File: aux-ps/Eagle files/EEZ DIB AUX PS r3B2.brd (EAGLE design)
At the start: 230.5 x 60 mm, 85 parts, among them IC1 BD00FC0WFP, IC2 MAX31760AEE+, J1 PF0030/PC, J2 4907, J3 4907, J4 4907, J5 SWEB 8094 AU/GN, Q1 BTA26-600, Q2 BTA26-600, Q3 2N7002, Q4 2N7002, Q5 2N7002, SW1 DF62J12S2AHQA, SW2 OS102011MA1QN1C, X1 39-28-1063, X2 39-30-1039, X3 DS1013-16SSIB1, X4 47053-1000, X5 47053-1000

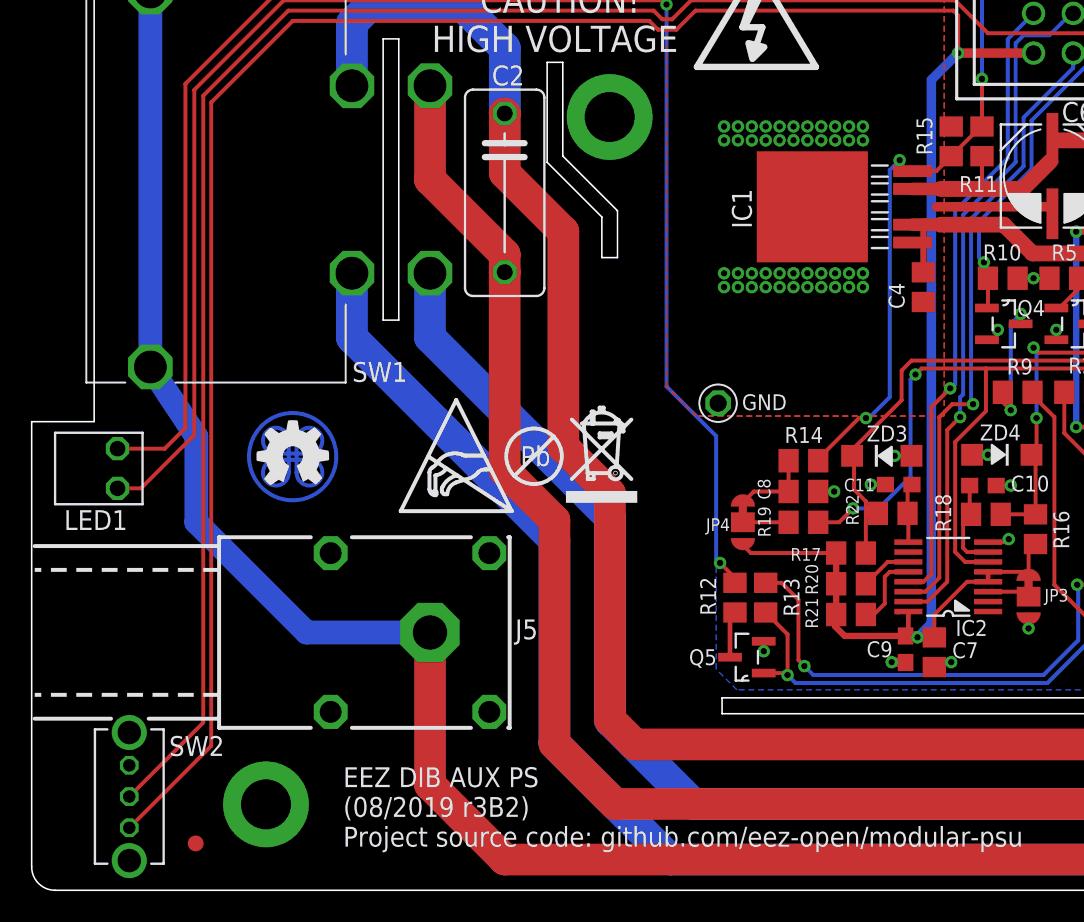
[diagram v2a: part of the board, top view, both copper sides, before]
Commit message: multiple PCB layout adjustments
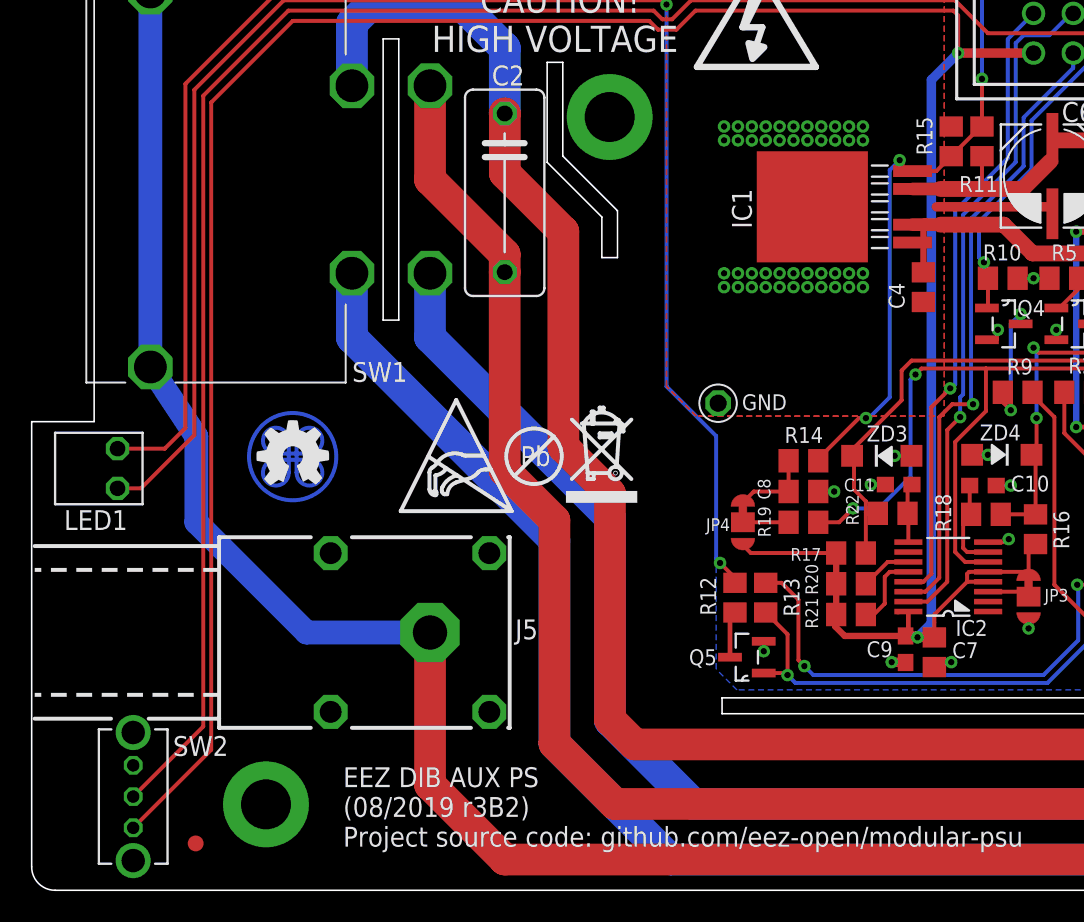
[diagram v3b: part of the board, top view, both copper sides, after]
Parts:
- moved SW2 0.25 mm to (6.50, 6.00)
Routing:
- net +3V3: track 177.1 -> 178.3 mm
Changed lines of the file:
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@@
 <layer number="27" name="tValues" color="14" fill="1" visible="no" active="yes"/>
 <layer number="28" name="bValues" color="11" fill="1" visible="yes" active="yes"/>
-<layer number="29" name="tStop" color="15" fill="1" visible="no" active="yes"/>
+<layer number="29" name="tStop" color="15" fill="1" visible="yes" active="yes"/>
 <layer number="30" name="bStop" color="7" fill="1" visible="yes" active="yes"/>
 <layer number="31" name="tCream" color="7" fill="4" visible="no" active="yes"/>
@@
 <layer number="49" name="Reference" color="7" fill="1" visible="no" active="yes"/>
 <layer number="50" name="dxf" color="7" fill="1" visible="no" active="no"/>
-<layer number="51" name="tDocu" color="14" fill="1" visible="no" active="yes"/>
+<layer number="51" name="tDocu" color="14" fill="1" visible="yes" active="yes"/>
 <layer number="52" name="bDocu" color="7" fill="1" visible="no" active="yes"/>
 <layer number="53" name="tGND_GNDA" color="7" fill="9" visible="no" active="no"/>
@@
 <wire x1="44.196" y1="12.319" x2="71.6915" y2="12.319" width="0.1016" layer="20"/>
 <wire x1="44.196" y1="11.303" x2="44.196" y2="12.319" width="0.1016" layer="20"/>
-<rectangle x1="84.8995" y1="0.889" x2="148.844" y2="5.588" layer="51"/>
 <wire x1="43.815" y1="14.224" x2="43.815" y2="29.083" width="0.254" layer="51"/>
 <wire x1="43.815" y1="29.083" x2="40.64" y2="32.258" width="0.254" layer="51"/>
 <wire x1="40.64" y1="32.258" x2="40.64" y2="35.433" width="0.254" layer="51"/>
+<dimension x1="0" y1="-13.5" x2="4" y2="1" x3="2" y3="-12.5" textsize="2" layer="47" dtype="horizontal"/>
 </plain>
 <attributes>
@@
 <attribute name="VALUE" x="128.1525" y="29.2345" size="2.1844" layer="27" ratio="10"/>
 </element>
-<element name="SW2" library="EEZ_switches" package="OS102011" value="OS102011MA1QN1C" x="6.25" y="6" locked="yes" smashed="yes" rot="R270">
-<attribute name="NAME" x="8.7955" y="8.5995" size="1.27" layer="25" ratio="10"/>
-<attribute name="VALUE" x="1.9375" y="5.361" size="1.27" layer="27" ratio="10"/>
+<element name="SW2" library="EEZ_switches" package="OS102011" value="OS102011MA1QN1C" x="6.5" y="6" locked="yes" smashed="yes" rot="R270">
+<attribute name="NAME" x="9.0455" y="8.5995" size="1.27" layer="25" ratio="10"/>
+<attribute name="VALUE" x="2.1875" y="5.361" size="1.27" layer="27" ratio="10"/>
 </element>
 <element name="D1" library="EEZ_Lib1" package="SOD123" value="SKL16" x="121.0945" y="56.5785" smashed="yes" rot="R270">
@@
 <contactref element="IC2" pad="5"/>
 <contactref element="JP3" pad="NC"/>
-<wire x1="61.2267" y1="20.3835" x2="61.2267" y2="19.7485" width="0.3048" layer="1"/>
 <wire x1="51.501" y1="21.59" x2="51.501" y2="19.6215" width="0.4064" layer="1"/>
 <wire x1="51.501" y1="19.6215" x2="51.501" y2="17.653" width="0.4064" layer="1"/>
 <contactref element="SW2" pad="3"/>
-<wire x1="6.25" y1="4" x2="11.4935" y2="9.2435" width="0.254" layer="1"/>
 <contactref element="JP4" pad="NO"/>
 <contactref element="X3" pad="16"/>
@@
 <wire x1="51.435" y1="17.587" x2="51.501" y2="17.653" width="0.4064" layer="1"/>
 <wire x1="56.0705" y1="17.7927" x2="56.1213" y2="17.8435" width="0.3048" layer="1"/>
-<wire x1="11.4935" y1="9.2435" x2="11.4935" y2="50.4317" width="0.254" layer="1"/>
+<wire x1="11.4935" y1="8.9935" x2="11.4935" y2="50.4317" width="0.254" layer="1"/>
 <wire x1="11.4935" y1="50.4317" x2="16.7132" y2="55.6514" width="0.254" layer="1"/>
 <wire x1="16.7132" y1="55.6514" x2="39.5351" y2="55.6514" width="0.254" layer="1"/>
@@
 <wire x1="57.5945" y1="51.8795" x2="59.309" y2="53.594" width="0.6096" layer="16"/>
 <wire x1="57.5945" y1="17.0815" x2="56.7055" y2="16.1925" width="0.6096" layer="16"/>
+<wire x1="11.4935" y1="8.9935" x2="6.5" y2="4" width="0.254" layer="1"/>
+<wire x1="61.2267" y1="20.3835" x2="60.0075" y2="20.3835" width="0.254" layer="1"/>
+<wire x1="60.0075" y1="20.3835" x2="59.8805" y2="20.2565" width="0.254" layer="1"/>
+<wire x1="59.8805" y1="20.2565" x2="59.8805" y2="19.7485" width="0.254" layer="1"/>
 </signal>
 <signal name="SSCL">
@@
 <contactref element="SW2" pad="2"/>
 <contactref element="X3" pad="2"/>
-<wire x1="10.9855" y1="10.7355" x2="10.9855" y2="50.8635" width="0.254" layer="1"/>
-<wire x1="10.9855" y1="10.7355" x2="6.25" y2="6" width="0.254" layer="1"/>
+<wire x1="10.9855" y1="10.4855" x2="10.9855" y2="50.8635" width="0.254" layer="1"/>
 <wire x1="10.9855" y1="50.8635" x2="16.4338" y2="56.3118" width="0.254" layer="1"/>
 <wire x1="16.4338" y1="56.3118" x2="39.8145" y2="56.3118" width="0.254" layer="1"/>
@@
 <wire x1="61.214" y1="54.864" x2="59.1058" y2="56.9722" width="0.254" layer="1"/>
 <wire x1="42.2148" y1="56.9722" x2="59.1058" y2="56.9722" width="0.254" layer="1"/>
+<wire x1="10.9855" y1="10.4855" x2="6.5" y2="6" width="0.254" layer="1"/>
 </signal>
 <signal name="12V_PWM">

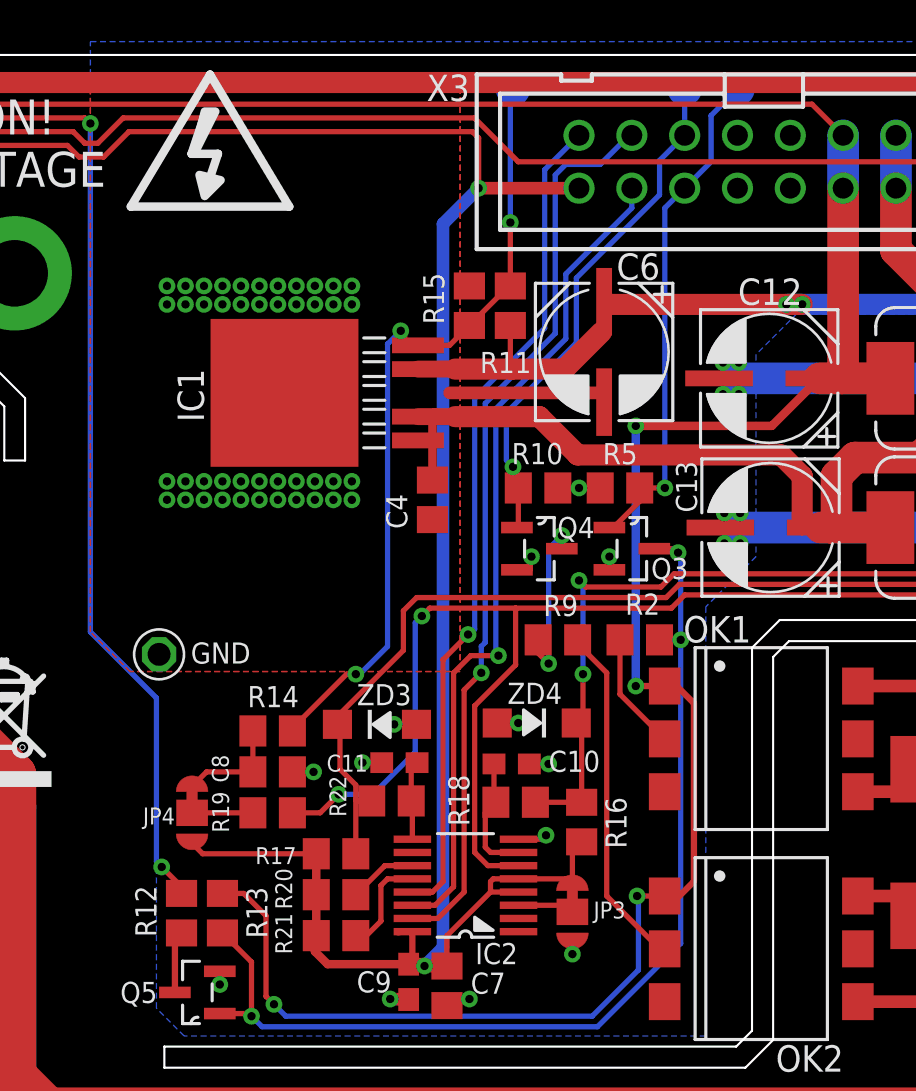
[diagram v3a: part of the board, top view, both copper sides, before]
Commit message: Fan LDO control fixed
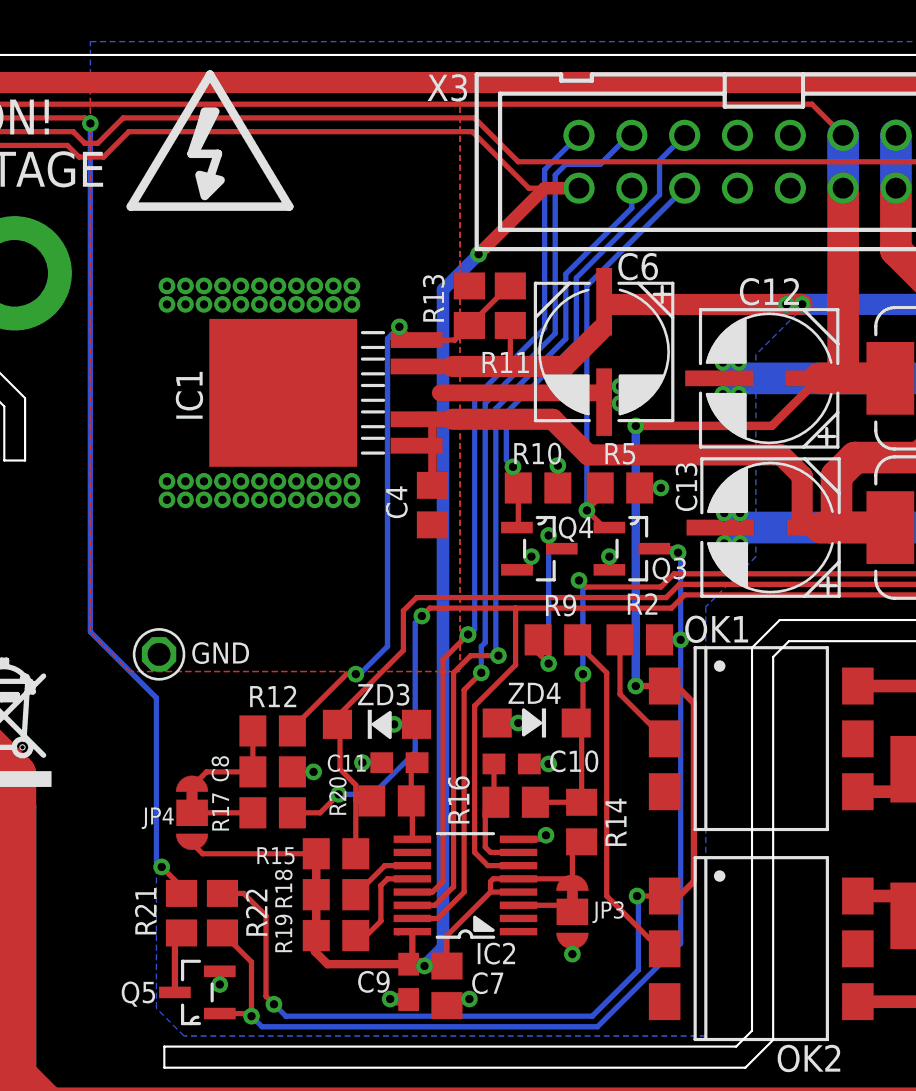
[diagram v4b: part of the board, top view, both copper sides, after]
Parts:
- removed DIR, FB, SS: (no value), EEZ_Lib1:PCB_TEST_PAD
- D1: value SKL16 -> SKL14
- IC1: value BD00FC0WFP -> BD00FC0WFP-E2; device EEZ_DIB:KVU5 -> EEZ_DIB:TO-252-5
- R11: value 10K -> 39K
- R12: value 470R -> 12K
- R13: value 47K -> 3K3
- R14: value 47K -> 1K
- R15: value 4K7 -> 1K
- R16: value 1K -> 10R
- R18: value 10R -> 4K7
- R19: value 1K -> N.C.
- R20: value 4K7 -> 10R
- R21: value N.C. -> 470R
- R22: value 10R -> 47K
- moved R13 31.5 mm to (58.9, 47.9), turned to 90 degrees
- moved R15 27.1 mm to (52.5, 21.6), turned to 180 degrees
- moved R14 15.5 mm to (64.3, 23.1), turned to 270 degrees
- moved R12 9.80 mm to (49.4, 27.5), turned to 180 degrees
- moved R22 9.76 mm to (47.0, 18.7), turned to 270 degrees
- moved R18 9.71 mm to (52.5, 19.6), turned to 180 degrees
- moved R21 7.51 mm to (45.0, 18.7), turned to 270 degrees
- moved R19 6.65 mm to (52.5, 17.7), turned to 180 degrees
- moved R20 5.24 mm to (55.1, 24.1)
- moved R17 3.63 mm to (49.4, 23.6), turned to 0 degrees
- moved R16 3.31 mm to (61.1, 24.1), turned to 0 degrees
- moved C4 0.25 mm to (57.1, 38.4)
- moved IC1 0.06 mm to (49.9, 43.8)
- turned R5 to 180 degrees
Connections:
- net +3V3: now also R14.2, R15.2, R18.2, R19.2; no longer R16.2, R17.2, R20.2, R21.2
- net +5V: now also R22.1; no longer R13.1
- net FAN_SENSE1: now also R14.1, R16.2; no longer R16.1, R18.2
- net FAN_SENSE2: now also R15.1, R20.2; no longer R17.1, R22.2
- net GND: now also R13.2; no longer R15.2
- net LDO_FB: now also R12.1, R13.1; no longer FB.NC, R14.1, R15.1
- net N$13: now also R21.2; no longer R12.2
- net N$14: now also R21.1; no longer R12.1
- net N$18: now also R18.1; no longer R20.1
- net N$2: now also R16.1; no longer R18.1
- net N$21: now also R20.1; no longer R22.1
- net N$3: now also R19.1; no longer R21.1
- net N$4: now also R17.1; no longer R19.1
- net N$9: now also R12.2; no longer R14.2
- net PWM_OUT: now also R17.2; no longer R19.2
- net PWR_DIRECT: no longer DIR.NC
- net PWR_DIR_OUT: now also R22.2; no longer R13.2
- net PWR_SSTART: no longer SS.NC
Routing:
- net LDO_FB: track 38.6 -> 28.7 mm, vias 3 -> 2
- net PWR_DIRECT: track 24.5 -> 20.5 mm
- net PWR_SSTART: track 25.7 -> 23.4 mm
- net +3V3: track 178.3 -> 179.9 mm
- net GND: track 196.2 -> 196.8 mm, vias 67 -> 70

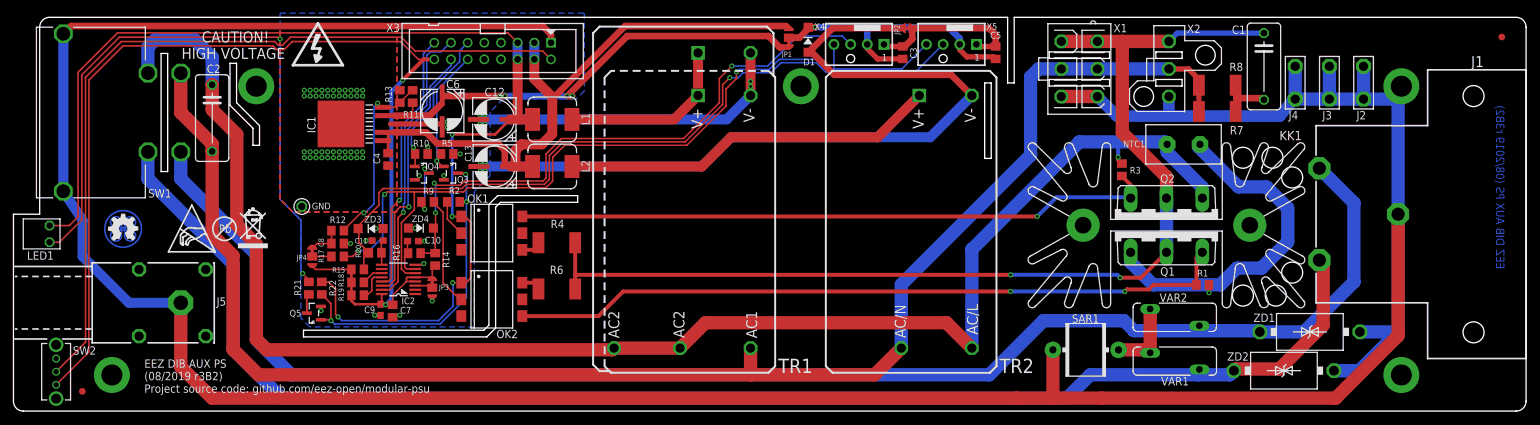
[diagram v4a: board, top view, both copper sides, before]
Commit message: AUX PS PWM pullup added
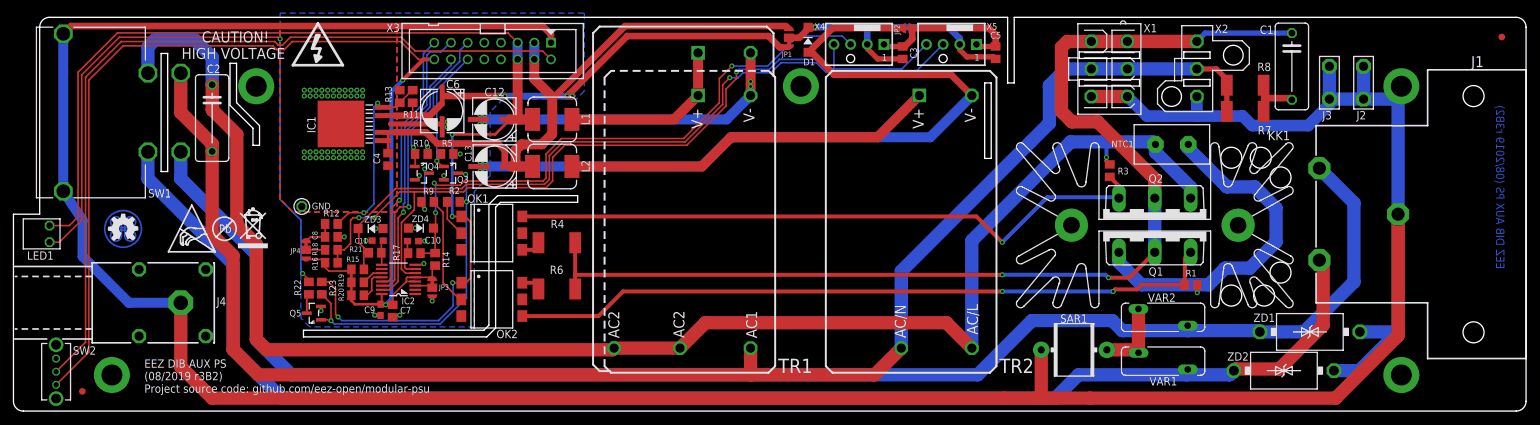
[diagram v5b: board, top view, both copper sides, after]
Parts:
- removed J5: SWEB 8094 AU/GN, EEZ_Lib1:S16N-PC
- added R23: 47K, rcl:R0805
- C11: value 100n -> N.C.
- C5: value 1u -> N.C.
- J4: value 4907 -> SWEB 8094 AU/GN; device EEZ_connectors:PCB_TAB-4907 -> EEZ_Lib1:S16N-PC
- R12: value 12K -> 3K3
- R16: value 10R -> 4K7
- R17: value 1K -> 10R
- R18: value 4K7 -> 1K
- R19: value N.C. -> 4K7
- R20: value 10R -> N.C.
- R21: value 470R -> N.C.
- R22: value 47K -> 470R
- X5: value 47053-1000 -> N.C.
- moved J4 173.1 mm to (25.5, 16.5), turned to 180 degrees
- moved R16 12.7 mm to (48.5, 22.6), turned to 180 degrees
- moved R17 11.7 mm to (61.1, 24.1)
- moved R21 11.4 mm to (55.1, 24.1), turned to 180 degrees
- moved R20 7.00 mm to (52.5, 17.7)
- moved R18 6.37 mm to (48.5, 24.6), turned to 0 degrees
- moved X1 4.57 mm to (167.0, 52.1)
- moved C1 4.25 mm to (194.8, 52.5)
- moved X2 4.25 mm to (180.3, 52.1)
- moved R7 4.25 mm to (187.7, 45.7)
- moved R8 4.25 mm to (187.7, 49.7)
- moved R19 1.97 mm to (52.5, 19.6)
- moved R22 1.97 mm to (45.0, 18.7)
- moved R3 1.85 mm to (167.1, 36.6)
- moved R1 1.78 mm to (179.5, 19.2)
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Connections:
- net +3V3: now also R16.2, R20.2; no longer R18.2
- net +5V: now also R23.1; no longer R22.1
- net FAN_SENSE1: now also R17.2; no longer R16.2
- net FAN_SENSE2: now also R21.2; no longer R20.2
- net N$13: now also R22.2; no longer R21.2
- net N$14: now also R22.1; no longer R21.1
- net N$18: now also R19.1; no longer R18.1
- net N$2: now also R17.1; no longer R16.1
- net N$21: now also R21.1; no longer R20.1
- net N$3: now also R20.1; no longer R19.1
- net N$4: now also R18.1; no longer R17.1
- net PE: now also J4.NC1, J4.NC2, J4.NC3, J4.NC4; no longer J4.2, J5.1, J5.NC1, J5.NC2, J5.NC3, J5.NC4
- net PWM_OUT: now also R16.1, R18.2; no longer R17.2
- net PWR_DIR_OUT: now also R23.2; no longer R22.2
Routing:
- net AC_OUT_L: track 165.3 -> 172.6 mm
- net PE: track 484.2 -> 477.4 mm
- net +3V3: track 179.9 -> 181.9 mm
- net AC_N_OUT: track 235.8 -> 237.6 mm
- net N$72: track 110.0 -> 108.3 mm
- net N$71: track 98.0 -> 99.3 mm
- net FAN_SENSE2: track 114.6 -> 113.5 mm
- net PWM_OUT: track 129.9 -> 131.0 mm
- net AC_L_OUT: track 239.9 -> 239.0 mm
- net LDO_FB: track 28.7 -> 29.3 mm
